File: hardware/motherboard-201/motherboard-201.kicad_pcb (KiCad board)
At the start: 2 copper layers, 216 x 150 mm, 114 parts, among them J1 PWR_conn, J2 DB25M, J3 MSX_Slot, J4 MSX_Slot, J5 GFX_Connector_Output, J6 CONN_JOY, J7 CONN_JOY, J8 DIN8, K1 Relay, Q1 2N2222, Q2 2N2907, SW1 Push_button, U1 AS6C1008, U10 74HC04, U11 74HC32, U12 74HC32, U13 74HC32, U14 74HC08, U15 74HC139, U16 74LS07, U17 74HC74, U19 LM311, U20 SST39SF0, U21 74HC138, U22 74HC138, U23 74HC157, U24 AY-3-8910, U25 74HC157, U26 74HC138, U27 74HC153, U28 82C55A, U6 Z84C00, U7 74HC74, U8 74HCT245, U9 74HCU04, Y1 3.58Mhz

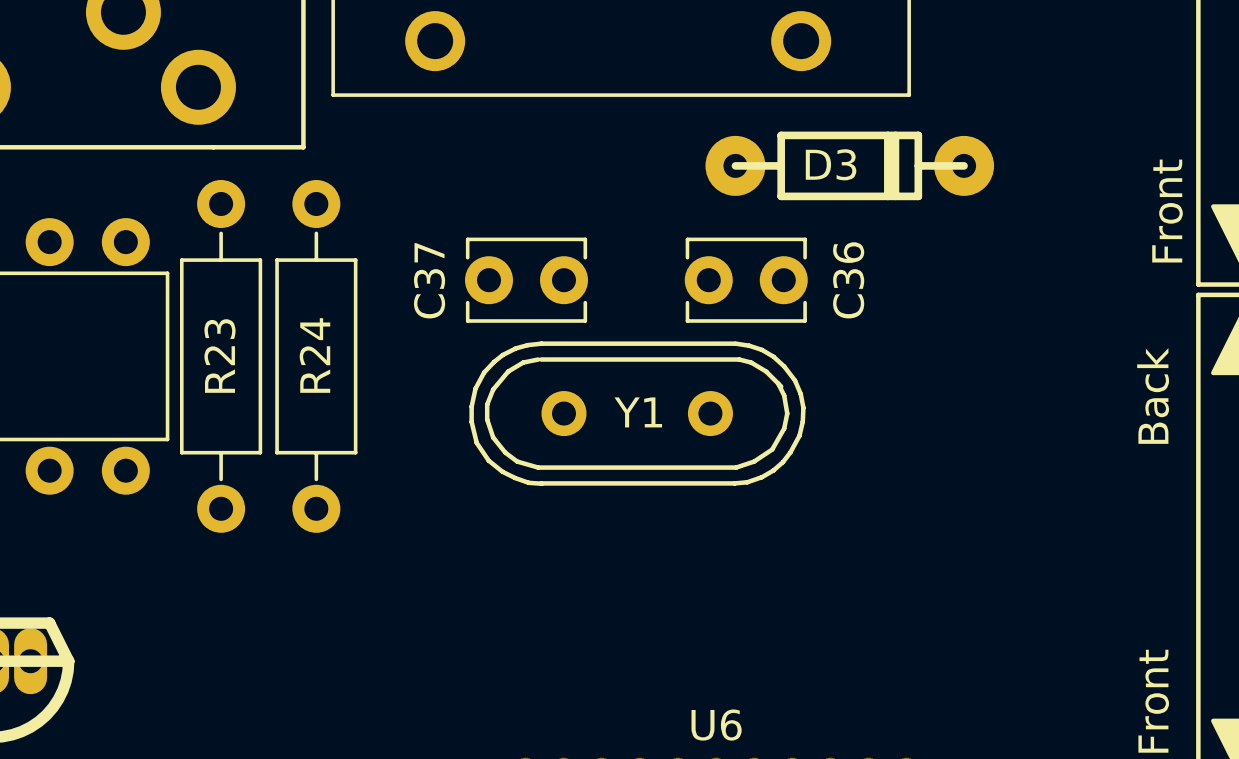
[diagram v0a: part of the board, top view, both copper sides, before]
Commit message: Replace clock circuit by an encapsulated oscillator SG7050
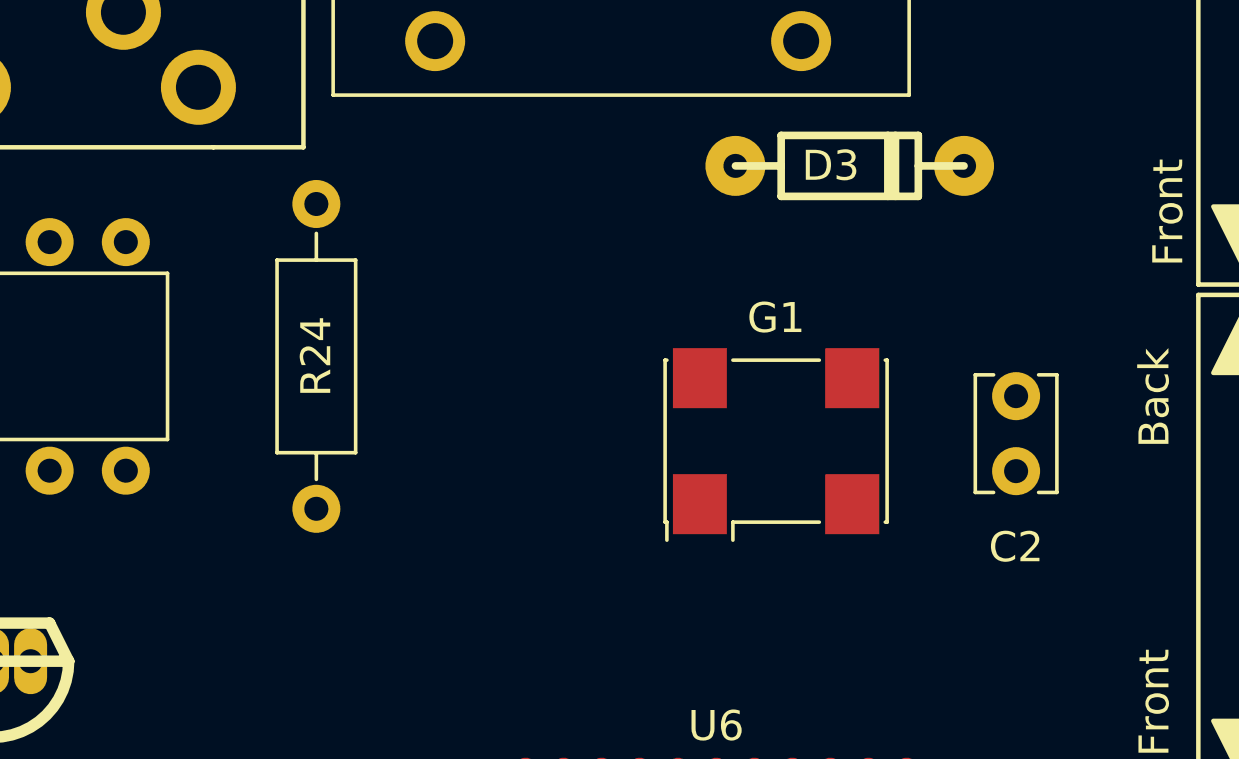
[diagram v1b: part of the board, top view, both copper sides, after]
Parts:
- removed C36, C37: 33pF, artemisa:Disc_capacitor
- removed R23: 1M, artemisa:Axial_resistor
- removed Y1: 3.58Mhz, artemisa:Crystal
- added C2: 100nF, artemisa:Disc_capacitor, F.Cu at (146.9, 108.6)
- added G1: SG7050, artemisa:SG7050, F.Cu at (138.9, 107.6)
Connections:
- U9 pad 10: Net-(U9-Pad10) -> (no net)
- U9 pad 11: Net-(R23-Pad2) -> (no net)
- U9 pad 12: /CLK -> (no net)
- U9 pad 13: Net-(U9-Pad10) -> (no net)
- U9 pad 8: Net-(R23-Pad2) -> (no net)
- U9 pad 9: Net-(C36-Pad1) -> (no net)

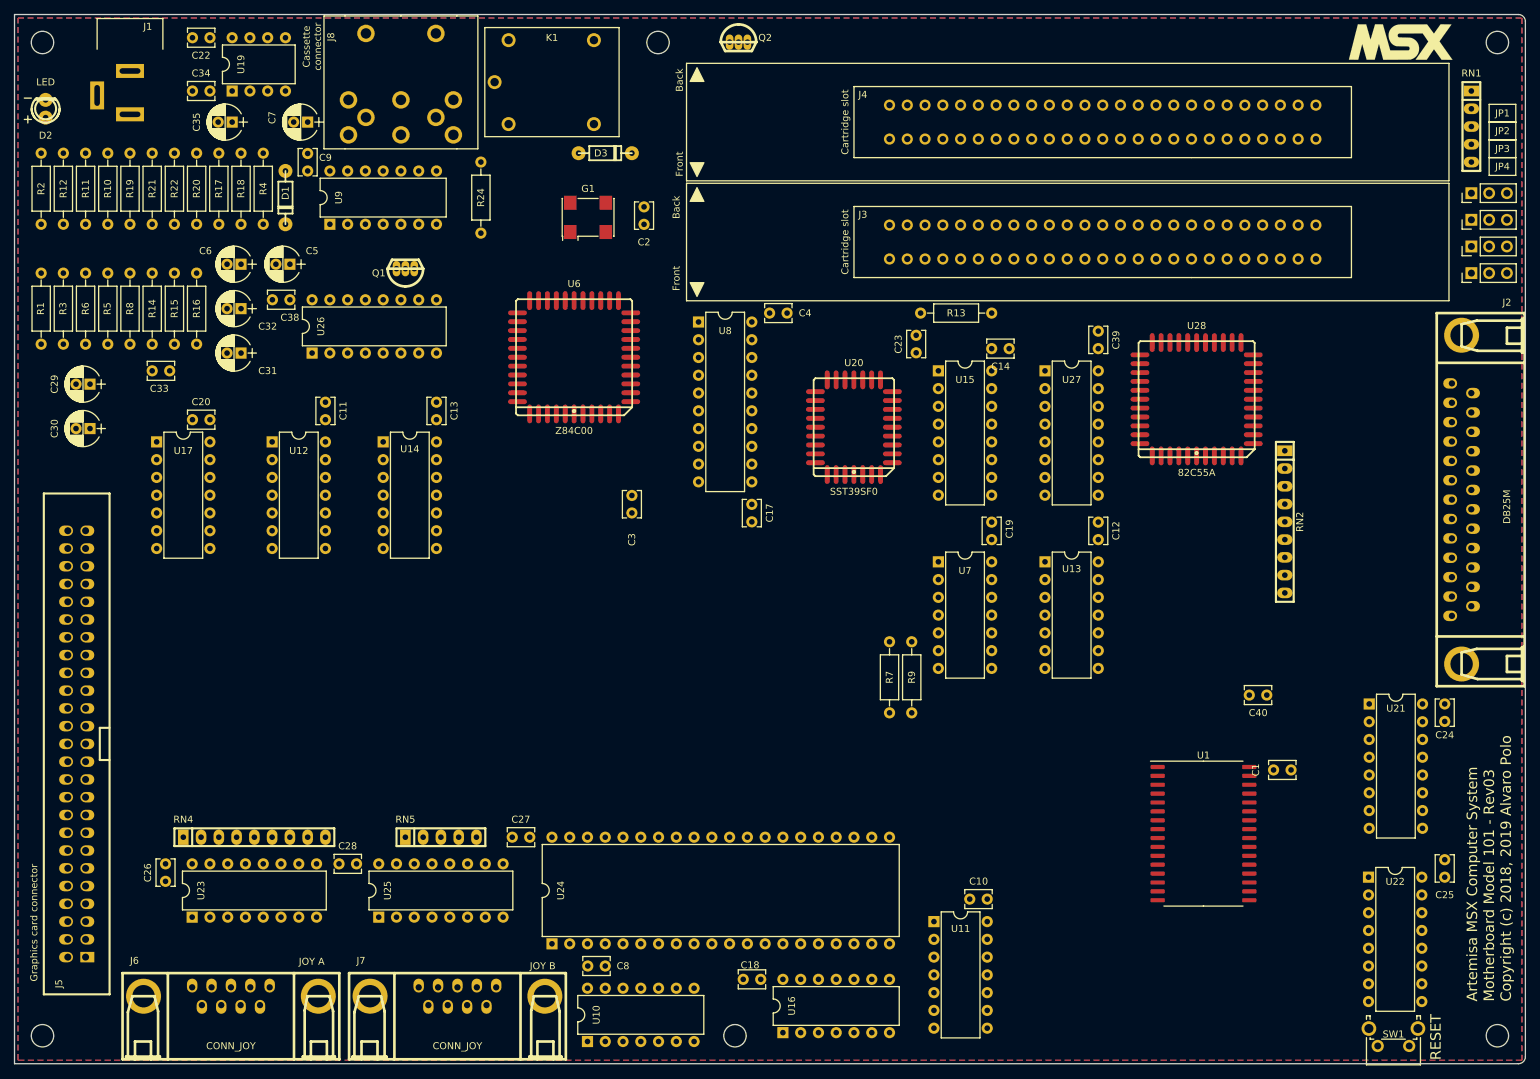
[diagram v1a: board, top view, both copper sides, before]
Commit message: Replace the custom power-on reset circuit by TL7705
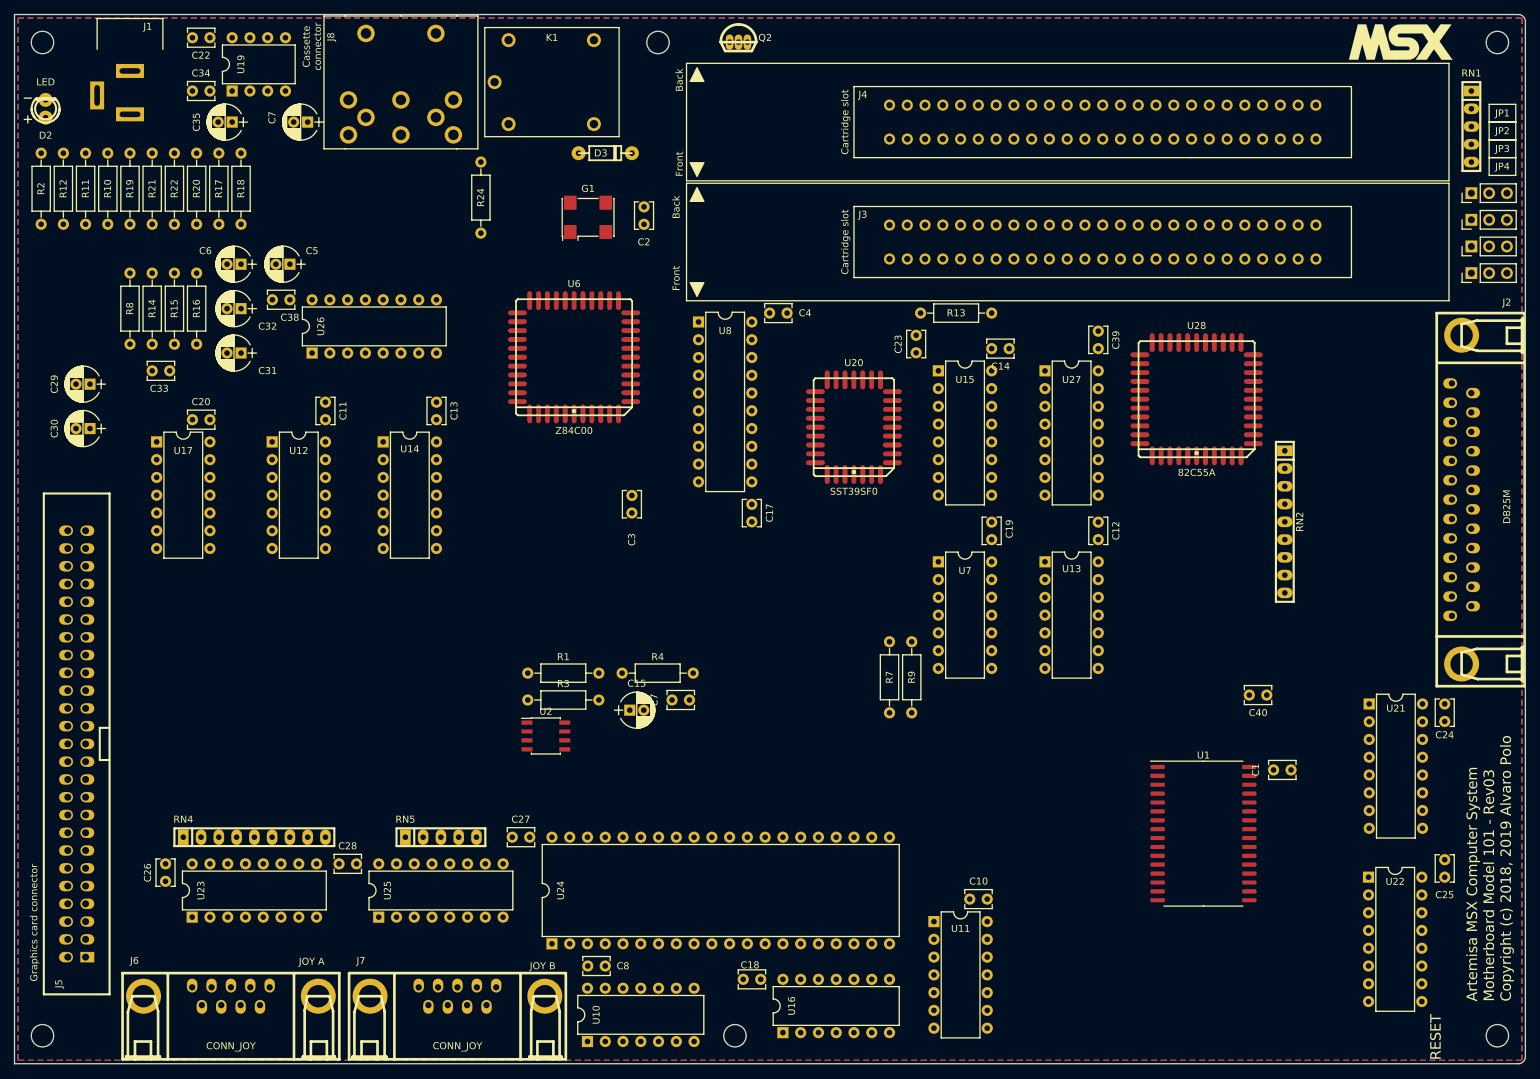
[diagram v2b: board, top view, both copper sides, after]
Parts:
- removed C9: 100nF, artemisa:Disc_capacitor
- removed D1: 1N4448, artemisa:Axial_diode
- removed Q1: 2N2222, artemisa:TO92
- removed R5: 1K, artemisa:Axial_resistor
- removed R6: 4K7, artemisa:Axial_resistor
- removed SW1: Push_button, artemisa:Push_button_angled
- removed U9: 74HCU04, artemisa:DIP-14_300
- added C15: 1uF, artemisa:Radial_capacitor, F.Cu at (144.9, 178.1)
- added C7: 100nF, artemisa:Disc_capacitor, F.Cu at (150.9, 176.6)
- added U2: TL7705, artemisa:SOIC-8_150, F.Cu at (132.9, 181.7)
- R1: value 100K -> 10K
- R3: value 4K7 -> 560
- moved R4 90.3 mm to (143.8, 172.8), turned to 0 degrees
- moved R3 90.2 mm to (130.3, 176.6), turned to 0 degrees
- moved R1 90.1 mm to (130.3, 172.8), turned to 0 degrees
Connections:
- R1 pad 1: Net-(R1-Pad1) -> ~
- R1 pad 2: Net-(Q1-Pad2) -> /~RESET
- R3 pad 1: ~ -> Net-(R3-Pad1)
- R4 pad 1: ~ -> GND
- R4 pad 2: Net-(C7-Pad1) -> /RESET

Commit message: Use 1206 packages for resistors and ceramic caps
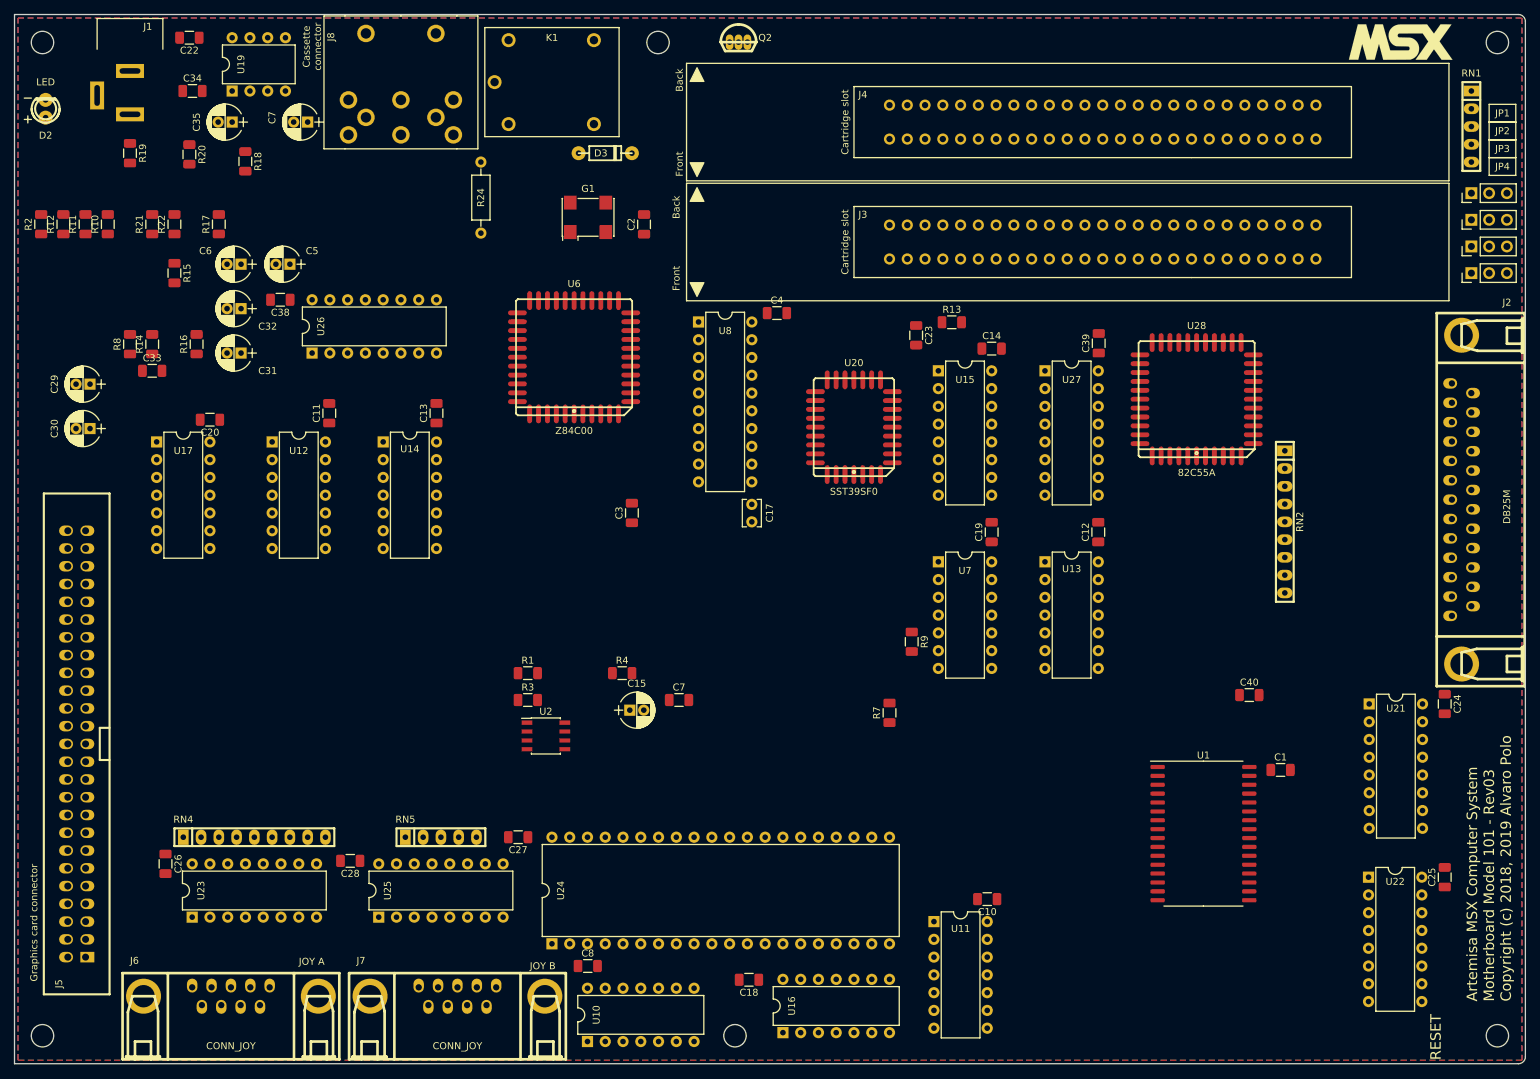
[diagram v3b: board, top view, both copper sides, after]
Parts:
- C1, C10, C11, C12, C13, C14, C18, C19, C2, C20, C22, C23, C24, C25, C26, C27, C28, C3, C33, C34, C38, C39, C4, C40, C7, C8: footprint artemisa:Disc_capacitor -> artemisa:C_1206
- R1, R10, R11, R12, R13, R14, R15, R16, R17, R18, R19, R2, R20, R21, R22, R3, R4, R7, R8, R9: footprint artemisa:Axial_resistor -> artemisa:R_1206
- moved R13 4.65 mm to (190.9, 122.6)
- moved C22 2.94 mm to (81.9, 81.9)
- moved C18 1.68 mm to (161.9, 216.6)
- moved C27 1.66 mm to (128.9, 196.2)
- moved C38 1.37 mm to (94.9, 119.4)
- moved R18 1.33 mm to (89.9, 99.6)
- moved C11 1.08 mm to (101.9, 135.6)
- moved C12 1.07 mm to (211.8, 152.6)
- moved C19 1.07 mm to (196.6, 152.6)
- moved C4 1.05 mm to (165.9, 121.3)
- moved R20 1.05 mm to (81.9, 98.6)
- moved C1 1.00 mm to (237.9, 186.6)
- moved C7 1.00 mm to (151.9, 176.6)
- moved C28 0.99 mm to (104.9, 199.6)
- moved C13 0.93 mm to (117.2, 135.6)
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
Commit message: Use ceramic capacitor for C15We actually have access to 1nF values in SMD encapsulation.
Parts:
- C15: footprint artemisa:Radial_capacitor -> artemisa:C_1206
